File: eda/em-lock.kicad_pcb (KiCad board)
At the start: 2 copper layers, 55.9 x 55.9 mm, 75 parts, among them CON1 BARREL_JACK, P1 EXT_LED_CONN, P10 BOOT_SEL_CONN, P12 SWD_CONN, P2 RC522A, P3 RC522B, P4 BTN_OPEN, P5 BTN_CALL, P6 ESP8266_CONN, P7 LOCK_CONN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

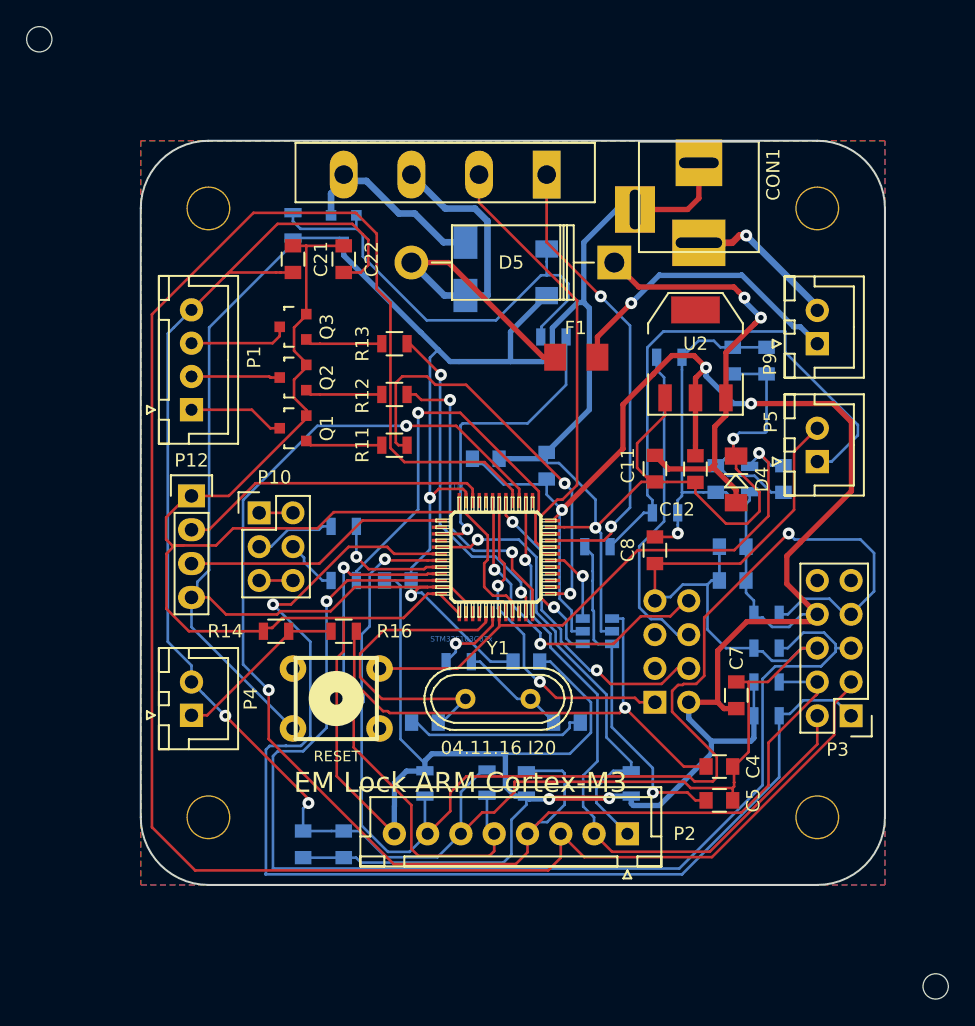
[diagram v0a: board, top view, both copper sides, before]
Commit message: refs #41563 +leds multiplexor + leds pcb's
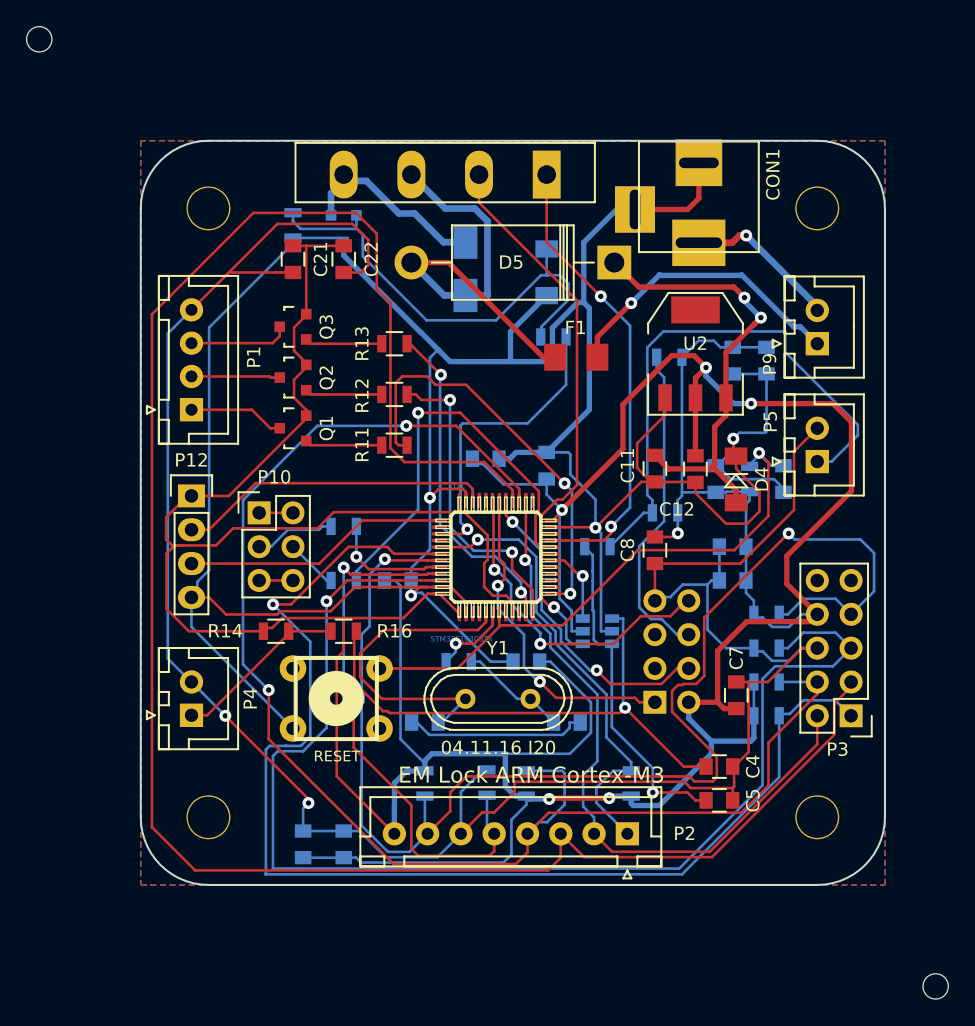
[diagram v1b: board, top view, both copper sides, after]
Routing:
- net PB9_RC522B_IRQ: track 92.4 -> 93.3 mm

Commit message: fix PCB before manufacturing
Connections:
- C1 pad 2: GNDD -> GND
- C14 pad 2: Net-(C14-Pad2) -> GND
- C15 pad 2: Net-(C14-Pad2) -> GND
- C2 pad 2: GNDD -> GND
- C21 pad 2: GNDD -> GND
- C22 pad 2: GNDD -> GND
- C3 pad 2: GNDD -> GND
- C4 pad 1: GNDD -> GND
- C5 pad 1: GNDD -> GND
- C6 pad 2: GNDD -> GND
- C7 pad 1: GNDD -> GND
- C8 pad 1: GNDD -> GND
- P1 pad 4: GNDD -> GND
- P10 pad 5: Net-(P10-Pad5) -> GND
- P10 pad 6: Net-(P10-Pad5) -> GND
- P2 pad 6: GNDD -> GND
- P3 pad 10: (no net) -> Net-(P3-Pad10)
- P3 pad 6: GNDD -> GND
- P3 pad 9: (no net) -> Net-(P3-Pad9)
- P4 pad 2: GNDD -> GND
- P5 pad 2: GNDD -> GND
- P6 pad 3: (no net) -> Net-(P6-Pad3)
- P6 pad 5: (no net) -> Net-(P6-Pad5)
- P6 pad 7: GNDD -> GND
- R20 pad 1: GNDD -> GND
- R7 pad 1: GNDD -> GND
- U3 pad 10: (no net) -> Net-(U3-Pad10)
- U3 pad 14: (no net) -> Net-(U3-Pad14)
- U3 pad 15: (no net) -> Net-(U3-Pad15)
- U3 pad 16: (no net) -> Net-(U3-Pad16)
- U3 pad 17: (no net) -> Net-(U3-Pad17)
- U3 pad 2: (no net) -> Net-(U3-Pad2)
- U3 pad 25: (no net) -> Net-(U3-Pad25)
- U3 pad 3: (no net) -> Net-(U3-Pad3)
- U3 pad 32: (no net) -> Net-(U3-Pad32)
- U3 pad 33: (no net) -> Net-(U3-Pad33)
- U3 pad 38: (no net) -> Net-(U3-Pad38)
- U3 pad 4: (no net) -> Net-(U3-Pad4)
- U3 pad 40: (no net) -> Net-(U3-Pad40)
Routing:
- net GND: track 241.9 -> 514.6 mm, vias 4 -> 17
- net GNDD: track 171.5 -> 0.00 mm, vias 2 -> 0
- net VCC: track 348.9 -> 473.8 mm, vias 6 -> 20
- net Net-(C14-Pad2): track 13.7 -> 0.00 mm
- net PB15_SPI2_MOSI: track 150.8 -> 143.5 mm
- net Net-(P10-Pad5): track 2.54 -> 0.00 mm
- net Net-(D3-Pad1): track 34.9 -> 36.6 mm
- net PB7_RC522_RST: track 101.6 -> 100.0 mm
- net PB6_RC522B_CS: track 91.4 -> 90.6 mm
- net PB14_SPI2_MISO: track 110.4 -> 111.1 mm
- net PB9_RC522B_IRQ: track 93.3 -> 92.6 mm
- added copper zone on B.Cu, net GND
- removed copper zone on B.Cu, net GNDD
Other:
- board text added: "18.12.16 I20"
- board text added: "Pavel Ruban"
- board text added: "Samarin Roman"
- board text removed: "04.11.16 I20"

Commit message: add new files
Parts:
- moved H8 12.8 mm to (40.8, 78.7)
- moved H9 8.76 mm to (86.5, 149.9)
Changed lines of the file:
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@@
     (links 158)
     (no_connects 0)
-    (area 35.484999 86.284999 91.515001 142.315001)
+    (area 29.236999 73.7 142.327 155.040001)
     (thickness 1.6)
-    (drawings 39)
+    (drawings 33)
     (tracks 1064)
     (zones 0)
@@
     (47 F.CrtYd user hide)
     (48 B.Fab user hide)
-    (49 F.Fab user hide)
+    (49 F.Fab user)
   )
   (setup
@@
     (pad_drill 0.762)
     (pad_to_mask_clearance 0.2)
-    (aux_axis_origin 46.736 79.756)
-    (grid_origin 52.832 80.01)
+    (aux_axis_origin 29.337 154.94)
+    (grid_origin 29.337 154.94)
     (visible_elements FFFFFFFF)
     (pcbplotparams
-      (layerselection 0x00100_7ffffffe)
+      (layerselection 0x20000_7ffffffe)
       (usegerberextensions false)
       (excludeedgelayer false)
@@
       (viasonmask true)
       (mode 1)
-      (useauxorigin false)
+      (useauxorigin true)
       (hpglpennumber 1)
       (hpglpenspeed 20)
@@
       (drillshape 0)
       (scaleselection 1)
-      (outputdirectory ""))
+      (outputdirectory manufacturing/cam/))
   )
   (net 0 "")
@@
   )
   (module I20:MountingHole_1.9mm locked (layer F.Cu)
-    (at 95.25 149.86)
+    (at 86.487 149.86)
     (descr "Mounting Hole 1.9mm")
     (tags "mounting hole 1.9mm")
@@
   )
   (module I20:MountingHole_1.9mm locked (layer F.Cu)
-    (at 27.94 78.74)
+    (at 40.767 78.74)
     (descr "Mounting Hole 1.9mm")
     (tags "mounting hole 1.9mm")
@@
     (tags "Diode Mini-MELF Standard")
     (attr smd)
-    (fp_text reference D4 (at 3.528 0 360) (layer F.SilkS)
+    (fp_text reference D4 (at 3.528 0) (layer F.SilkS)
       (effects (font (size 1 1) (thickness 0.15)))
     )
@@
     )
   )
+  (target plus (at 139.827 76.2) (size 5) (width 0.15) (layer Edge.Cuts))
+  (gr_line (start 97.282 154.94) (end 29.337 154.94) (layer F.Fab) (width 0.2))
   (gr_text "Samarin Roman" (at 64.516 108.204) (layer F.SilkS)
     (effects (font (size 1.2 1.2) (thickness 0.3)))
@@
     (effects (font (size 1.2 1.2) (thickness 0.3)))
   )
-  (gr_line (start 21.59 71.12) (end 20.32 71.12) (layer F.Fab) (width 0.2))
-  (gr_line (start 91.44 71.12) (end 21.59 71.12) (layer F.Fab) (width 0.2))
-  (gr_line (start 106.68 71.12) (end 91.44 71.12) (layer F.Fab) (width 0.2))
-  (gr_line (start 106.68 71.12) (end 125.73 71.12) (layer F.Fab) (width 0.15))
-  (gr_line (start 125.73 157.48) (end 106.68 157.48) (layer F.Fab) (width 0.15))
+  (gr_line (start 97.282 74.93) (end 29.337 74.93) (layer F.Fab) (width 0.2))
   (gr_text "18.12.16 I20" (at 64.262 110.744) (layer F.SilkS)
     (effects (font (size 1 1) (thickness 0.25)))
@@
     (effects (font (size 1.2 1.2) (thickness 0.3)))
   )
-  (gr_line (start 20.32 71.12) (end 20.32 86.36) (layer F.Fab) (width 0.2))
-  (gr_line (start 125.73 157.48) (end 125.73 71.12) (layer F.Fab) (width 0.2))
-  (gr_line (start 31.75 157.48) (end 106.68 157.48) (layer F.Fab) (width 0.2))
-  (gr_line (start 20.32 157.48) (end 31.75 157.48) (layer F.Fab) (width 0.2))
-  (gr_line (start 20.32 86.36) (end 20.32 157.48) (layer F.Fab) (width 0.2))
-  (gr_line (start 92.71 157.48) (end 31.75 157.48) (layer F.Fab) (width 0.2))
+  (gr_line (start 97.282 154.94) (end 97.282 74.93) (layer F.Fab) (width 0.2))
+  (gr_line (start 29.337 74.93) (end 29.337 154.94) (layer F.Fab) (width 0.2))
   (gr_arc (start 40.64 137.16) (end 40.64 143.51) (angle 90) (layer Margin) (width 0.2))
   (gr_arc (start 86.36 137.16) (end 92.71 137.16) (angle 90) (layer Margin) (width 0.2))
